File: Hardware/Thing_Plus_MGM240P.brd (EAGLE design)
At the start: 22.9 x 58.4 mm, 128 parts, among them J1 THING_PLUS_LOGICAL, J2 USB Female Type C Connector, J3 QWIIC_RIGHT_ANGLE, J5 MICRO-SDFRICTION, Q1 20V/4.2A/52mΩ/1.4W, Q2 20V/4.2A/52mΩ/1.4W, U1 MGM240P, U2 XC6222B331MR-G, U4 MCP73831, U5 MAX17048, U6 MK22FN128VLH10

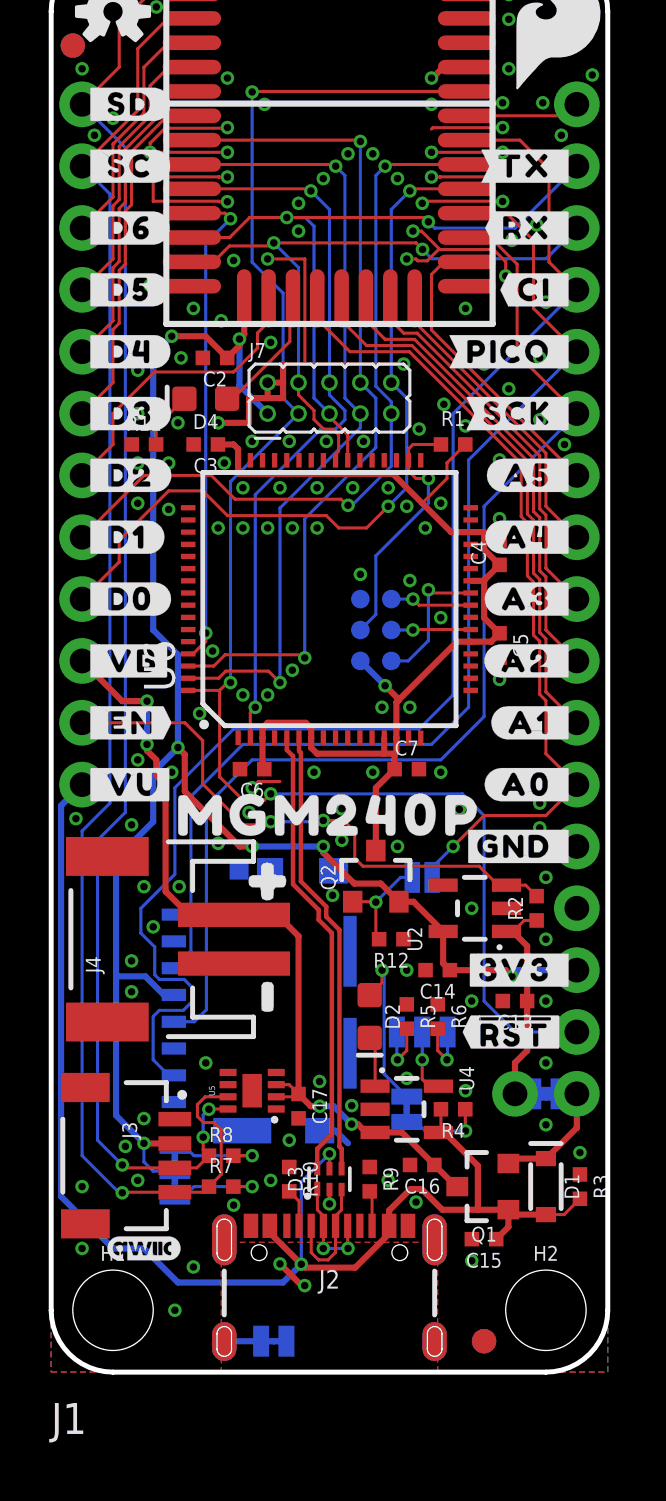
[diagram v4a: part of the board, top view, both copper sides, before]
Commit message: Design review updates
Add reset button
Add power LED
Pour USB shield on bottom too
Increase VUSB trace to 20mil
Add silk labels for LEDs
Add version number to copper
Change charge LED resistor value
Add "Thing Plus" to bottom silk
Add measures
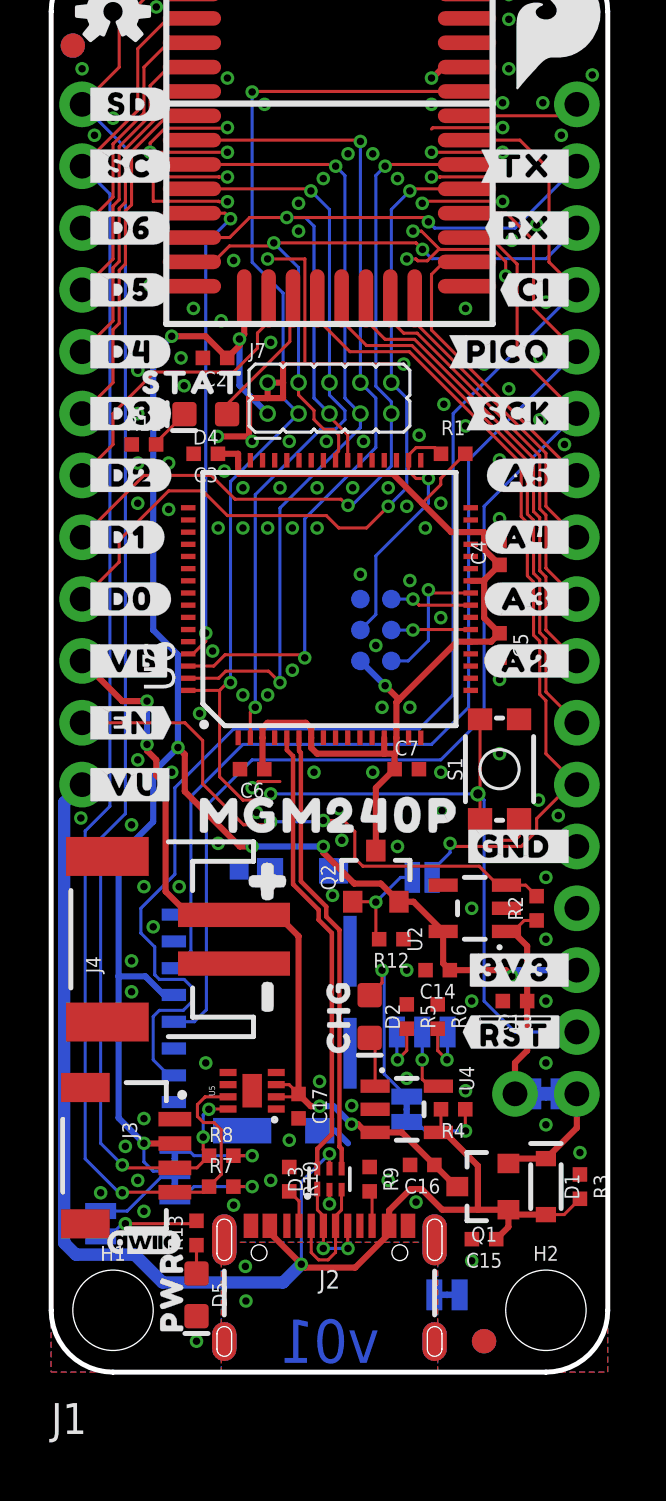
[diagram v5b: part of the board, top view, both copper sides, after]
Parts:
- added D5: RED, SparkFun-LED:LED-0603
- added PWR: JUMPER-SMT_2_NC_TRACE_SILK, SparkFun-Jumpers:SMT-JUMPER_2_NC_TRACE_SILK
- added R13: 1k, SparkFun-Resistors:0402-TIGHT
- added S1: MOMENTARY-SWITCH-SPST-SMD-4.6X2.8MM, SparkFun-Switches:TACTILE_SWITCH_SMD_4.6X2.8MM
- added U$67: (no value), output:CHG0
- added U$68: (no value), output:STAT0
- added U$69: (no value), output:THING_PLUS0
- R4: value 1k -> 4.7k
- U$19: device output:#A1_#0 -> output:#PWR#0
- U$20: device output:#A0_#0 -> output:PWR0
- moved U$19 27.7 mm to (2.03, 6.99), flipped to the bottom, turned to 90 degrees
- moved U$20 26.7 mm to (4.95, 3.30), turned to 90 degrees
- moved SHLD 7.36 mm to (16.3, 3.17)
- moved U$5 5.78 mm to (15.4, 3.17)
- moved FRAME1 3.81 mm to (-11.4, -22.9)
- moved D4 0.63 mm to (6.35, 39.3)
- moved C3 0.38 mm to (6.35, 37.7)
- moved R1 0.38 mm to (16.5, 37.7)
- moved LOGO2 0.25 mm to (3.81, 5.33)
- moved U$58 0.13 mm to (11.4, 33.8)
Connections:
- new net N$2: PWR.1, R13.2
- new net N$8: D5.A, R13.1
- net !RESET!: now also S1.3, S1.4
- net 3.3V: now also PWR.2
- net GND: now also D5.C, S1.1, S1.2
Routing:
- net !RESET!: track 64.1 -> 68.7 mm, vias 3 -> 4
- net N$2: track 0.00 -> 4.20 mm, vias 0 -> 1
- net 3.3V: track 72.7 -> 76.2 mm
- net SHLD: track 1.52 -> 0.00 mm, vias 0 -> 2
- net N$8: track 0.00 -> 1.16 mm
- net V_USB: track 57.2 -> 58.1 mm
- net VDD: track 44.6 -> 44.0 mm
- net GND: track 59.1 -> 59.7 mm
- net N$1: track 2.36 -> 1.73 mm
- net A0: track 33.6 -> 34.1 mm
- net LED: track 5.37 -> 5.88 mm
- added copper zone on layer 16, net SHLD
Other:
- board text added: "v01"

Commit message: Design review updates
Chang USB connector to 2-layer version
Fix gague typo in schematic
Remove UART flow control nets from J-Link
Spread out J-Link caps in schematic
Remove right angles from VDDJ trace and straighten out
Fix acid trap
Move reset button and 2 caps away from J-Link chip
Move POCI to top layer at SD card
Fix USB width before ESD protection
Thicker USB ESD trace
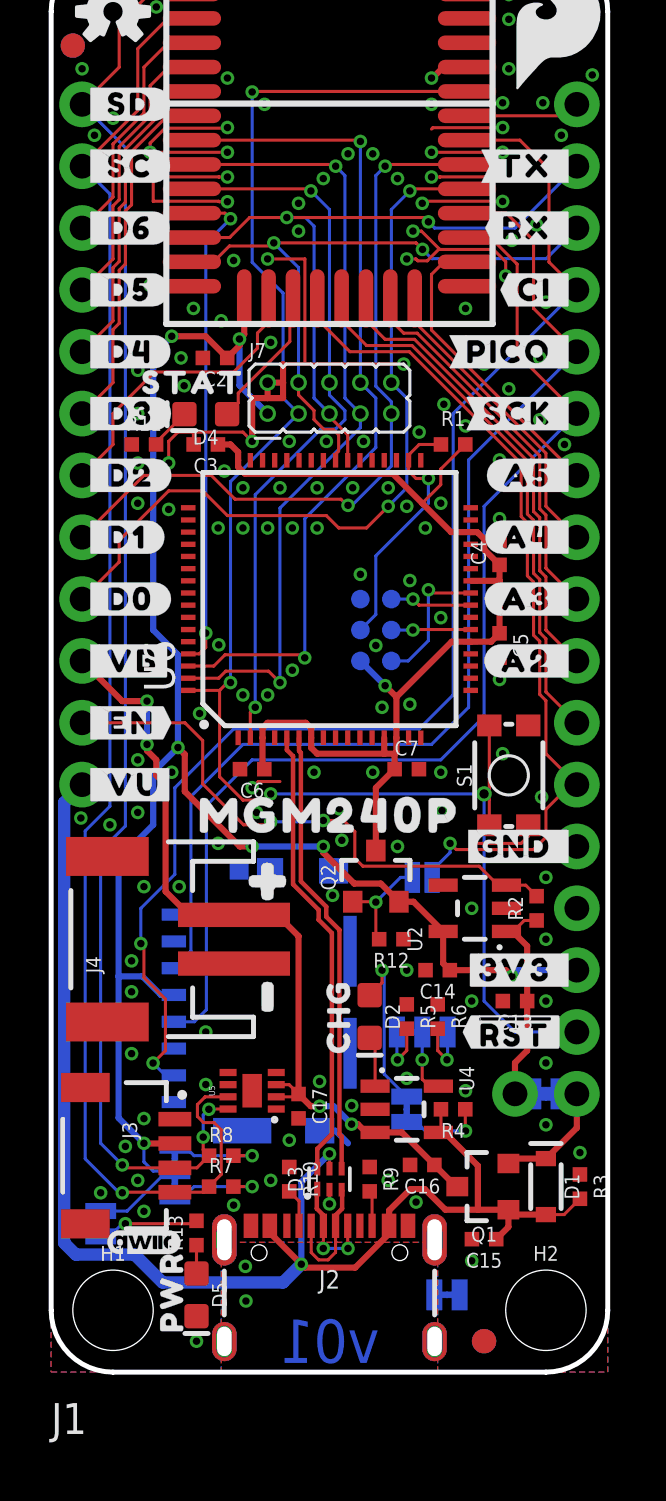
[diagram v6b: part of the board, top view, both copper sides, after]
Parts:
- J2: device SparkFun-Connectors:USB-C-16P-4LAYER-ISOLATED -> SparkFun-Connectors:USB-C-16P-2LAYER-PADS
- moved S1 0.46 mm to (18.8, 24.5)
- moved C3 0.38 mm to (6.35, 38.1)
- moved R1 0.38 mm to (16.5, 38.1)
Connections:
- removed net CTS: U6.38
- removed net RTS: U6.37
- net SHLD: no longer J2.SHLD5, J2.SHLD6, J2.SHLD7, J2.SHLD8
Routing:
- net GND: track 59.7 -> 65.0 mm
- net POCI: track 56.7 -> 54.6 mm, vias 0 -> 2

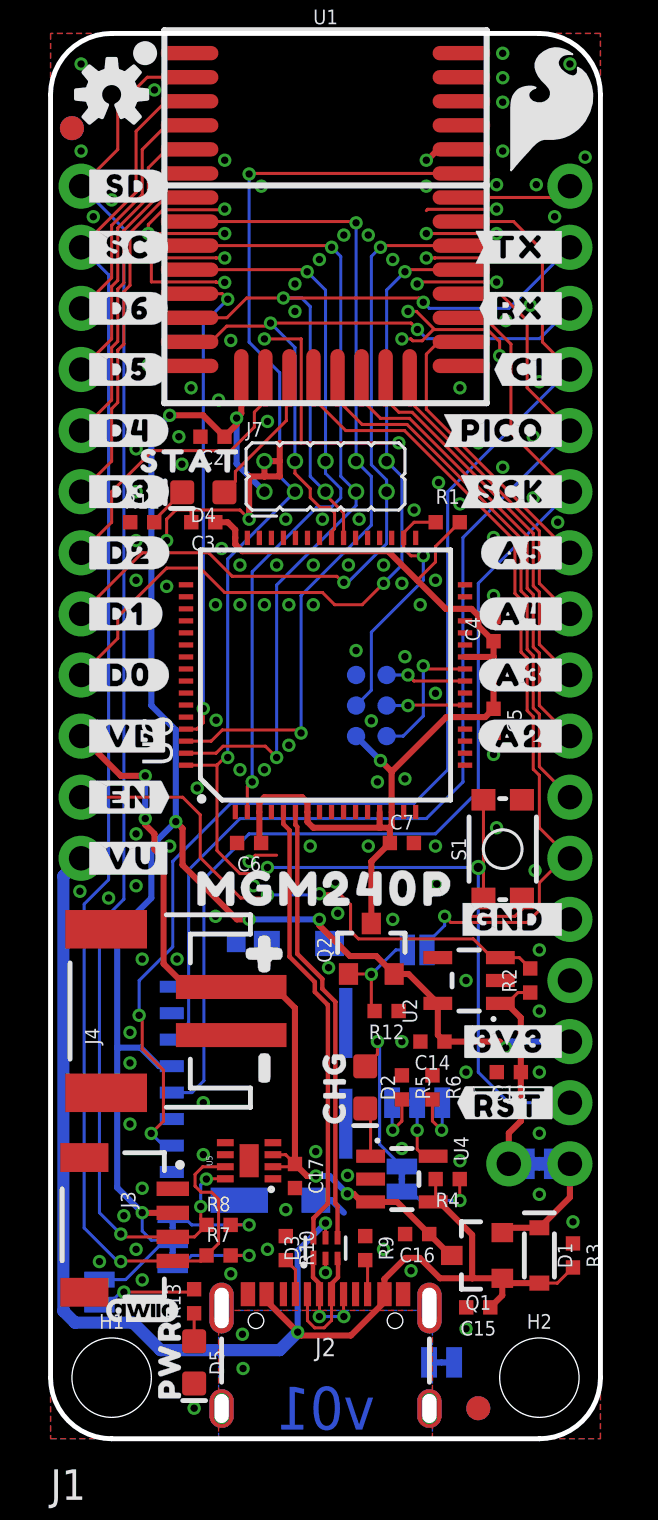
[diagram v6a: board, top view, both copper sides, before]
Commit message: Design review updates
Change to 4-layer board for better EMC and routing
Remove excessive GND vias now that it's 4 layers
Add label to reset button in silk
Add 10uF cap for SD card
Change net names to represent MGM240P port names rather than Arduino names
Connect uSD CS pin to PA07
Fix acid traps
Reposition MEAS to be off-grid to prevent confusion
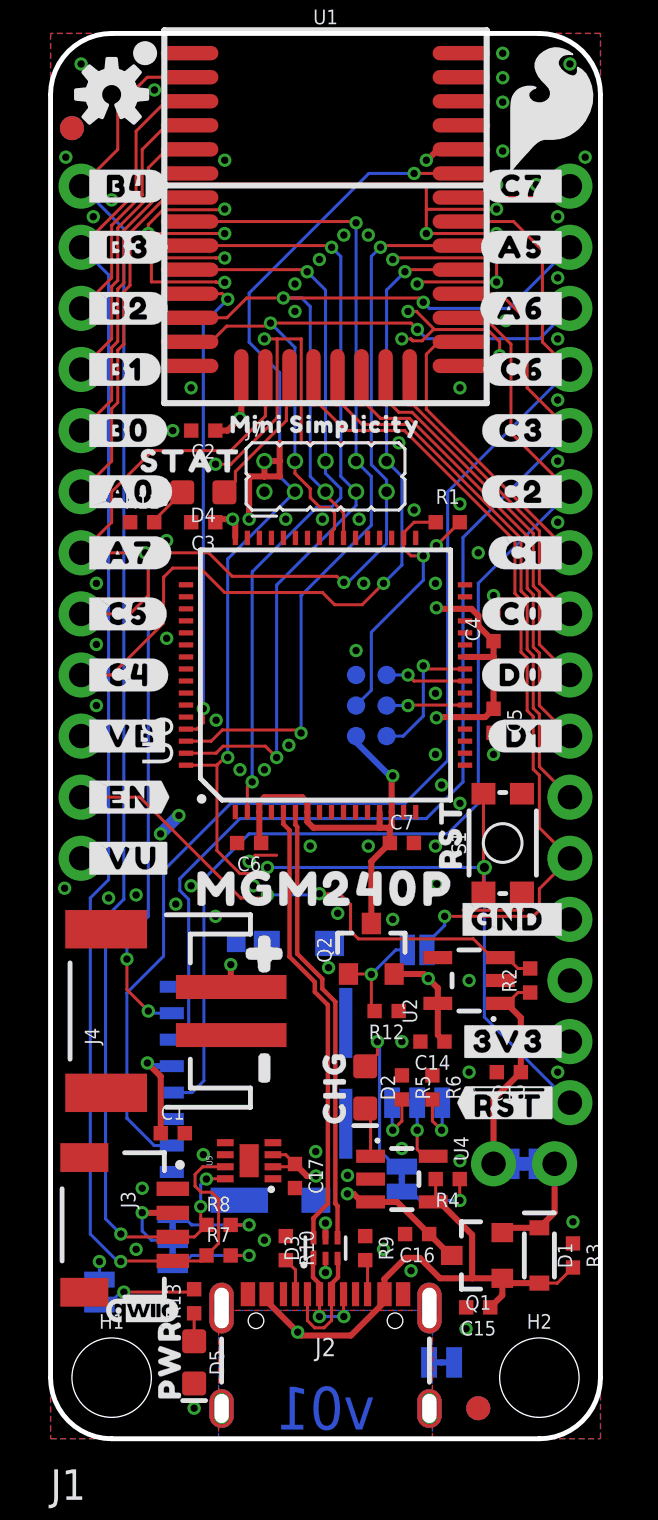
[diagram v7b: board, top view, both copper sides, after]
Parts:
- added C1: 10uF, SparkFun-Capacitors:0402-TIGHT
- added U$70: (no value), output:RST0
- added U$71: (no value), output:#_A5#TX#0
- added U$73: (no value), output:#SDA#B4_#0
- added U$74: (no value), output:#SCL#B3_#0
- U$1: device output:#_D6#0 -> output:#_B4#0
- U$10: device output:#_SC#0 -> output:#_C4#0
- U$11: device output:#TX_#0 -> output:#C7_#0
- U$12: device output:#RX_#0 -> output:#A5_#0
- U$13: device output:#PICO_#0 -> output:#A6_#0
- U$14: device output:#SCK_#0 -> output:#C6_#0
- U$15: device output:#A5_#0 -> output:#C3_#0
- U$16: device output:#A4_#0 -> output:#C2_#0
- U$17: device output:#A3_#0 -> output:#C1_#0
- U$18: device output:#A2_#0 -> output:#C0_#0
- U$2: device output:#_D5#0 -> output:#_B3#0
- U$24: device output:#CI_#0 -> output:#D0_#0
- U$3: device output:#_D4#0 -> output:#_B2#0
- U$32: device output:#_PICO#0 -> output:#D1_#0
- U$33: device output:#_POCI#0 -> output:#_C7#0
- U$34: device output:#_RX#0 -> output:#_A6#RX#0
- U$35: device output:#_TX#0 -> output:#_C6#POCI#0
- U$36: device output:#_SCK#0 -> output:#_C3#PICO#0
- U$37: device output:#_A5#0 -> output:#_C2#SCK#0
- U$38: device output:#_A4#0 -> output:MINI_SIMPLICITY0
- U$39: device output:#_A3#0 -> output:#_C1#0
- U$4: device output:#_D3#0 -> output:#_B1#0
- U$40: device output:#_A2#0 -> output:#_C0#0
- U$41: device output:#_A1#0 -> output:#_D0#0
- U$42: device output:#_A0#0 -> output:#_D1#0
- U$46: device output:#SDA_#0 -> output:#_D2#0
- U$47: device output:#SCL_#0 -> output:#_D3#0
- U$48: device output:#D6_#0 -> output:#C4_#0
- U$49: device output:#D5_#0 -> output:#C5_#0
- U$50: device output:#D4_#0 -> output:#A7_#0
- U$51: device output:#D3_#0 -> output:#A0_#0
- U$52: device output:#D2_#0 -> output:#B0_#0
- U$53: device output:#D1_#0 -> output:#B2_#0
- U$54: device output:#D0_#0 -> output:#B1_#0
- U$6: device output:#_D2#0 -> output:#_B0#0
- U$7: device output:#_D1#0 -> output:#_A0#0
- U$8: device output:#_D0#0 -> output:#_A7#0
- U$9: device output:#_SD#0 -> output:#_C5#0
- moved U$47 32.5 mm to (21.6, 24.1)
- moved U$46 32.5 mm to (21.6, 26.7)
- moved U$10 17.8 mm to (1.27, 31.8)
- moved U$9 17.8 mm to (1.27, 34.3)
- moved U$48 15.2 mm to (1.27, 31.8)
- moved U$38 12.9 mm to (11.4, 42.2), flipped to the top
- moved U$24 12.7 mm to (21.6, 31.8)
- moved U$53 12.7 mm to (1.27, 47.0)
- moved U$54 12.7 mm to (1.27, 44.5)
- moved U$32 12.7 mm to (21.6, 29.2), flipped to the top
- moved U$49 10.2 mm to (1.27, 34.3)
- moved U$33 7.62 mm to (21.6, 52.1)
- moved U$13 5.08 mm to (21.6, 47.0)
- moved U$14 5.08 mm to (21.6, 44.5)
- moved U$3 5.08 mm to (1.27, 47.0)
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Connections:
- net A0 renamed PD03
- net A1 renamed PD02
- net A2 renamed PD01
- net A3 renamed PD00
- net A4 renamed PC00
- net A5 renamed PC01
- net D3 renamed PA00
- net D4 renamed PB00
- net D5 renamed PB01
- net D6 renamed PB02
- net FREE renamed PC07
- net LED renamed LED/PA08
- net PICO renamed PICO/PC03
- net POCI renamed POCI/PC06
- net PTI_DATA/D0 renamed PTI_DATA/PC04
- net PTI_SYNC/D1 renamed PTI_SYNC/PC05
- net RX renamed RX/PA06
- net SCK renamed SCK/PC02
- net SCL renamed SCL/PB03
- net SDA renamed SDA/PB04
- net TCK/SWCLK renamed TCK/SWCLK/PA01
- net TDI renamed TDI/PA04
- net TDO/SWO renamed TDO/SWO/PA03
- net TMS/SWDIO renamed TMS/SWDIO/PA02
- net TX renamed TX/PA05
- removed net D2: J1.7, U1.16
- removed net N$37: J5.2
- new net PA07: J1.7, J5.2, U1.16
- net 3.3V: now also C1.1
- net GND: now also C1.2
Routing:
- net 3.3V: track 76.2 -> 16.8 mm
- net PA07: track 0.00 -> 35.9 mm, vias 0 -> 3
- net D2: track 12.3 -> 0.00 mm
- net GND: track 65.0 -> 69.9 mm, vias 150 -> 107
- net !RESET!: track 68.9 -> 64.6 mm
- net VDD: track 44.3 -> 46.3 mm, vias 1 -> 5
- net V_USB: track 58.1 -> 56.4 mm
- net EN: track 23.4 -> 22.4 mm
- net V_BATT: track 34.3 -> 33.4 mm, vias 4 -> 3
- net PTI_SYNC/PC05: track 31.1 -> 31.7 mm
- net PTI_DATA/PC04: track 32.2 -> 32.8 mm
- net POCI/PC06: vias 2 -> 0
- added copper zone on layer 15, net 3.3V
- added copper zone on layer 2, net GND
